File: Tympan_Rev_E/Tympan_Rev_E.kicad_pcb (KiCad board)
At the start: 4 copper layers, 38 x 74 mm, 84 parts, among them IC1 BC127, J1 SJ-3523-SMT-TR, J2 SJ-3524-SMT-TR-PI, P1 CONN_01X06, P2 CONN_01X06, P3 CONN_01X06, P4 CONN_01X06, P6 CONN_01X01, P7 CONN_01X01, P8 CONN_01X01, SW1 CL-SB-22A, U1 MCP73831, U2 TLV320AIC3206IRSBT, U3 74LVC1G66, U4 LP5907MFX-1.8, U5 Teensy4.1

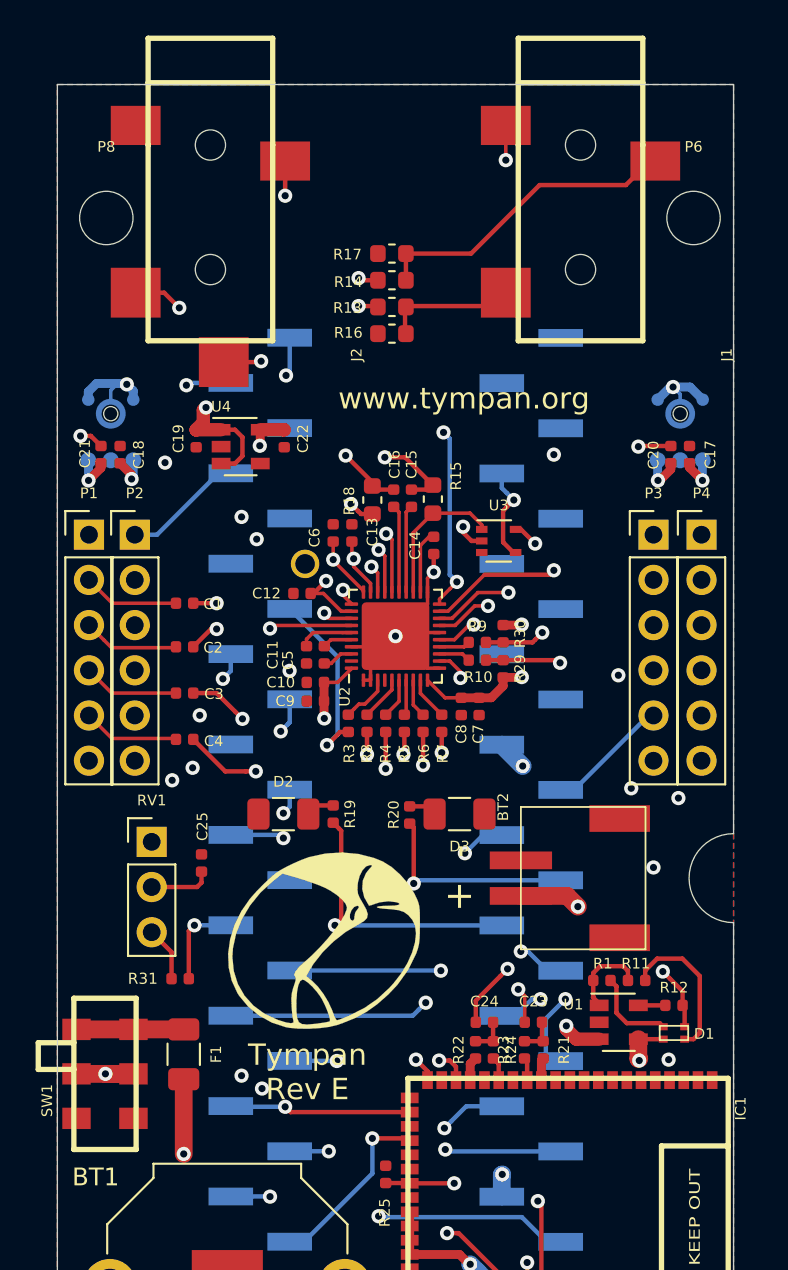
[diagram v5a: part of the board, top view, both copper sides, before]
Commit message: Re routing and adding gas guage
added gas guage and routed fuse per design rec in issue #6
added pullups to the I2C2 lines
cleaned silk and copper pours
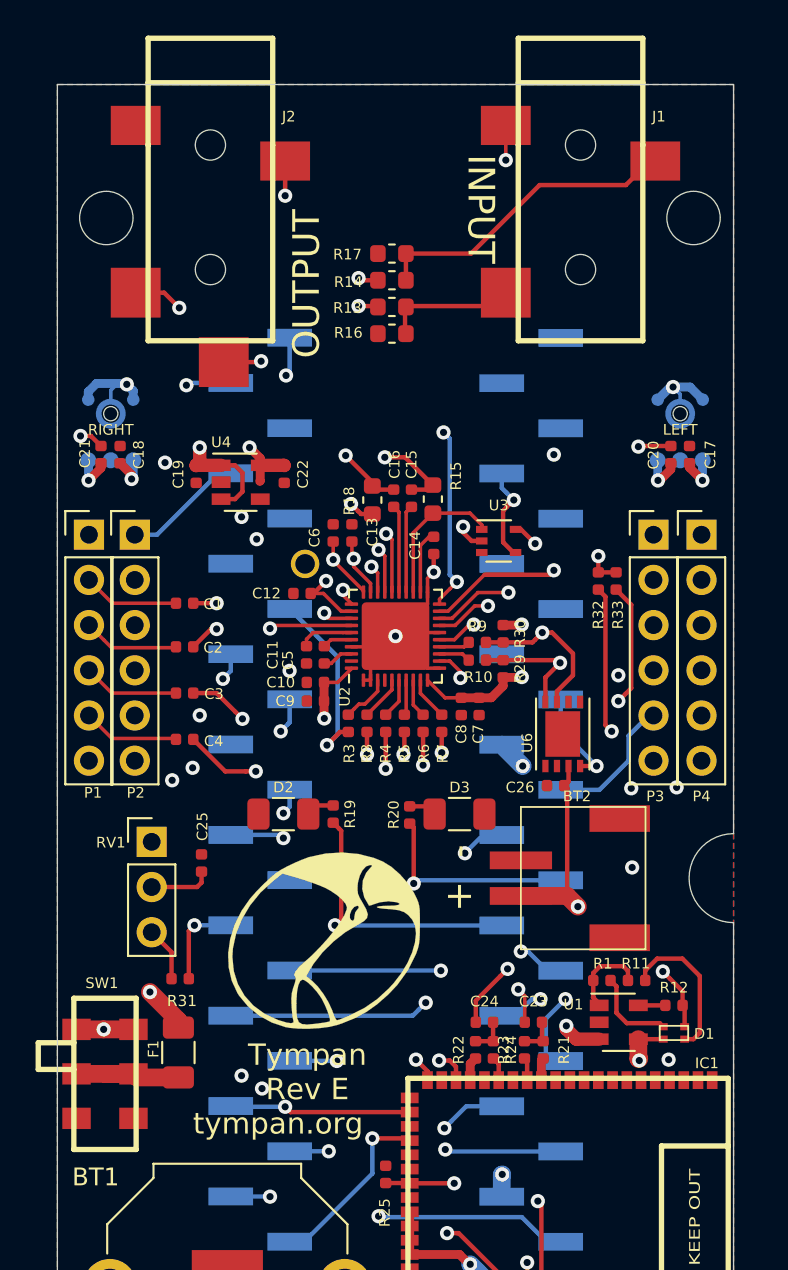
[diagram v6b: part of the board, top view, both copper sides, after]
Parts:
- added C26: 1uF, Capacitor_SMD:C_0402_1005Metric, F.Cu at (162.4, 98.6)
- added R32: 4K7, Resistor_SMD:R_0402_1005Metric, F.Cu at (164.8, 87.1)
- added R33: 4K7, Resistor_SMD:R_0402_1005Metric, F.Cu at (165.8, 87.1)
- added U6: LC709203, Tympan:WDFN8_3X4mm_0.65P, F.Cu at (162.8, 95.7)
- moved C19 2.00 mm to (142.2, 81.1)
- moved C22 2.00 mm to (147.2, 81.1)
- moved U4 2.00 mm to (144.7, 81.5)
- moved F1 0.32 mm to (141.2, 113.6), turned to 90 degrees
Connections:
- F1 pad 2: /VIN -> +BATT
- SW1 pad 1: Net-(F1-Pad1) -> /VIN
- SW1 pad 2: +BATT -> Net-(F1-Pad1)
- SW1 pad 4: Net-(F1-Pad1) -> /VIN
- SW1 pad 5: +BATT -> Net-(F1-Pad1)
- U5 pad 33: Net-(U5-Pad33) -> /ALARMB
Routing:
- net /SCL2: track 26.3 -> 34.5 mm, vias 1 -> 2
- net /SDA2: track 29.7 -> 36.6 mm, vias 1 -> 2
- net /ALARMB: track 0.00 -> 5.50 mm, vias 0 -> 1
- net /SDA: track 26.6 -> 31.9 mm
- net /SCL: track 27.9 -> 30.5 mm
- net +BATT: track 37.5 -> 40.0 mm
- net +3V3: track 36.7 -> 38.2 mm, vias 9 -> 10
- net Net-(F1-Pad1): track 6.03 -> 7.38 mm
- net +1V8: track 13.3 -> 14.6 mm
- net /VIN: track 12.4 -> 11.4 mm
- net /SCK: track 6.95 -> 7.77 mm
- net /SS: track 26.8 -> 26.1 mm
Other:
- board text added: "INPUT"
- board text added: "LEFT"
- board text added: "OUTPUT"
- board text added: "RIGHT"
- board text added: "tympan.org"
- board text removed: "www.tympan.org"

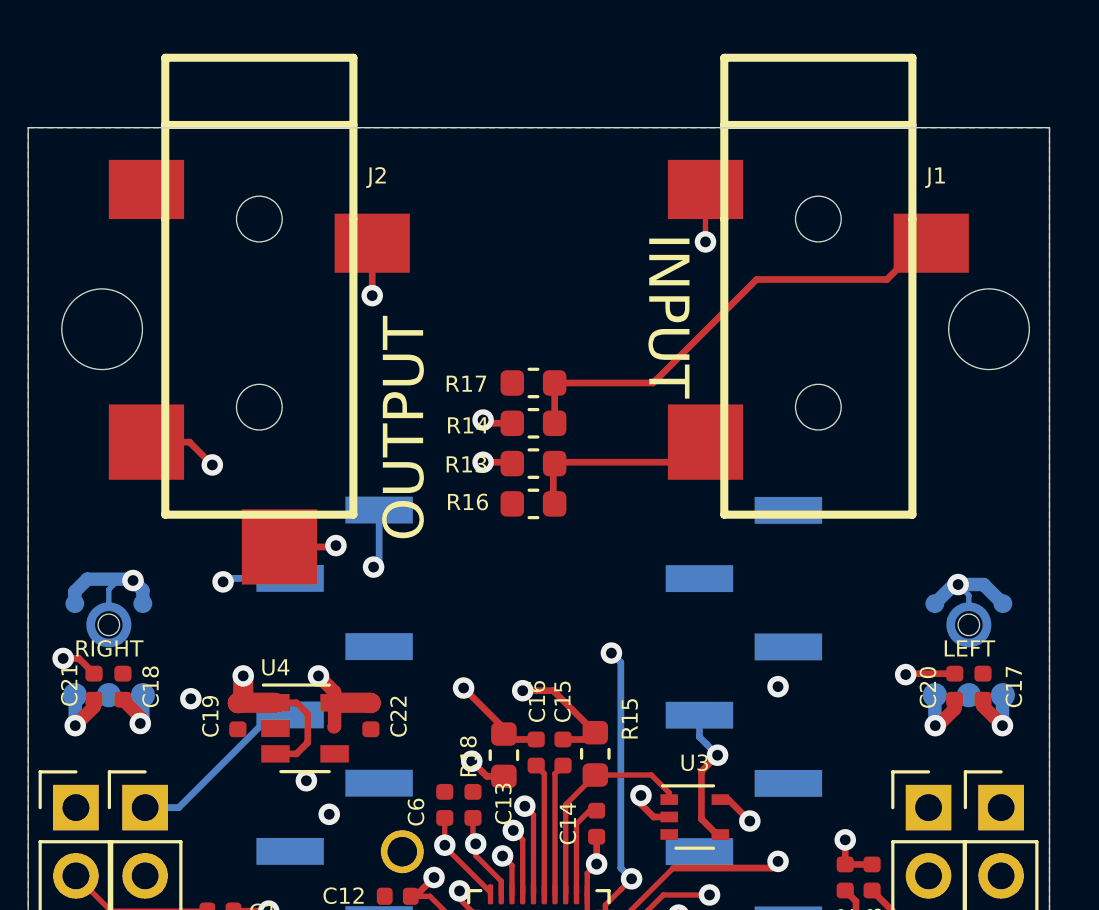
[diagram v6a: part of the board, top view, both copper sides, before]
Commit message: Added header for headphone connections
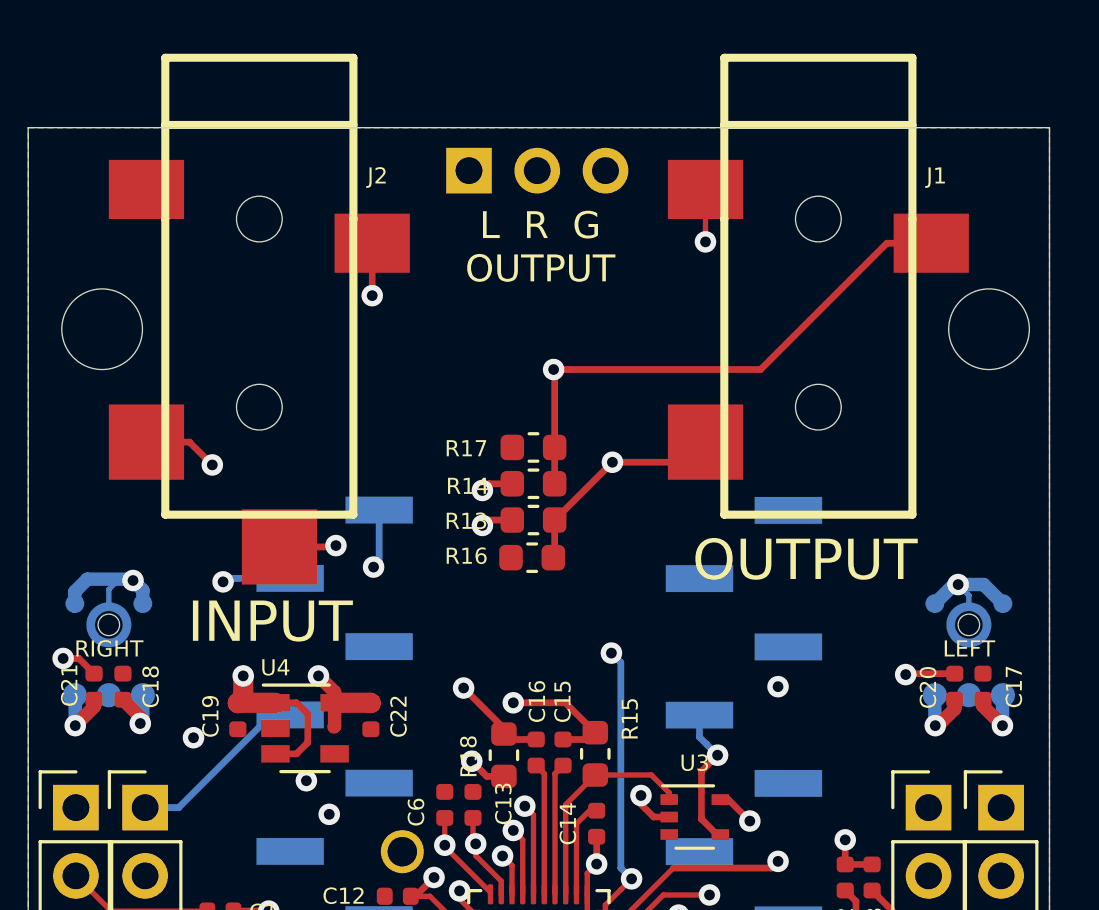
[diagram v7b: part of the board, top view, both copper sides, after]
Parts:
- added J3: Conn_01x03, Connector_PinHeader_2.54mm:PinHeader_1x03_P2.54mm_Vertical, B.Cu at (150.8, 60.8)
- moved R17 2.40 mm to (153.2, 71.1)
- moved R14 2.25 mm to (153.2, 72.5)
- moved G*** 2.20 mm to (153.4, 66.4)
- moved R13 2.10 mm to (153.2, 73.8)
- moved R16 2.00 mm to (153.2, 75.2)
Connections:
- net Net-(J1-Pad2) renamed /L
- net Net-(J1-Pad3) renamed /R
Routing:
- net /L: track 7.47 -> 21.3 mm, vias 0 -> 1
- net /R: track 17.7 -> 27.9 mm, vias 0 -> 1
- net /HPR: track 26.2 -> 23.7 mm
- net /HPL: track 21.6 -> 19.4 mm
- net Net-(C15-Pad2): track 29.2 -> 30.5 mm
- net /nRESET_1: track 24.5 -> 25.0 mm
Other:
- board text added: "L R G OUTPUT"

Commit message: tweaked the copper pours
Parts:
- moved G*** 0.55 mm to (153.4, 67.0)
- moved R18 0.47 mm to (152.2, 82.1)
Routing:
- net +BATT: track 40.0 -> 35.7 mm
- net /V_USB: track 29.2 -> 27.3 mm
- net /BT_nRESET: track 58.0 -> 56.8 mm
- net /IN1_L: track 46.6 -> 45.6 mm
- net /IN1_R: track 49.2 -> 50.0 mm
- net Net-(C15-Pad2): track 30.5 -> 31.2 mm
- net /SDA: track 31.9 -> 32.6 mm
- net GND: vias 11 -> 13
